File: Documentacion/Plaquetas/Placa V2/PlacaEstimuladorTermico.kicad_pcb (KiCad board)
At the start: 2 copper layers, 207.5 x 149.9 mm, 70 parts, among them J1 Conn_01x02, J2 DB9_Female_MountingHoles, J3 Conn_01x01, J4 Conn_01x01, J5 Conn_01x02, J6 Pulsador OFF, J7 Conn_02x04_Counter_Clockwise, J8 Conn_02x04_Counter_Clockwise, K1 Modulo_Relé, Q1 IRF4905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

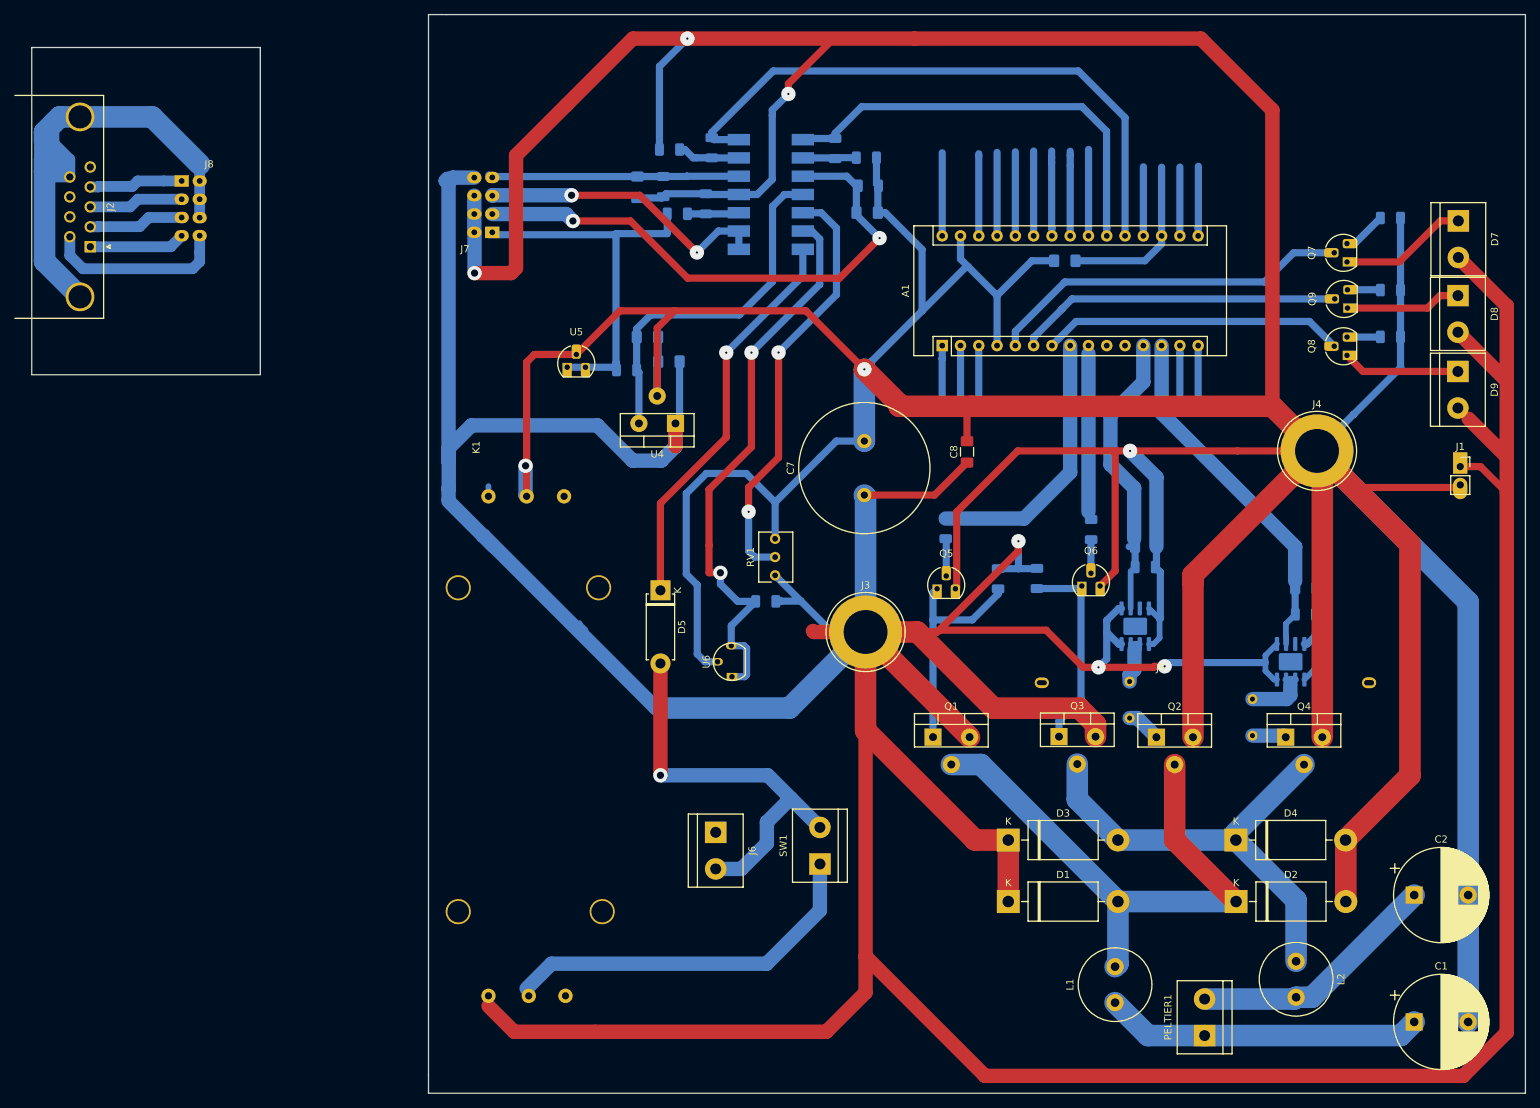
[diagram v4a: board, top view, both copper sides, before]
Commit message: Modification of the main board, add of leds circuit and db9 board
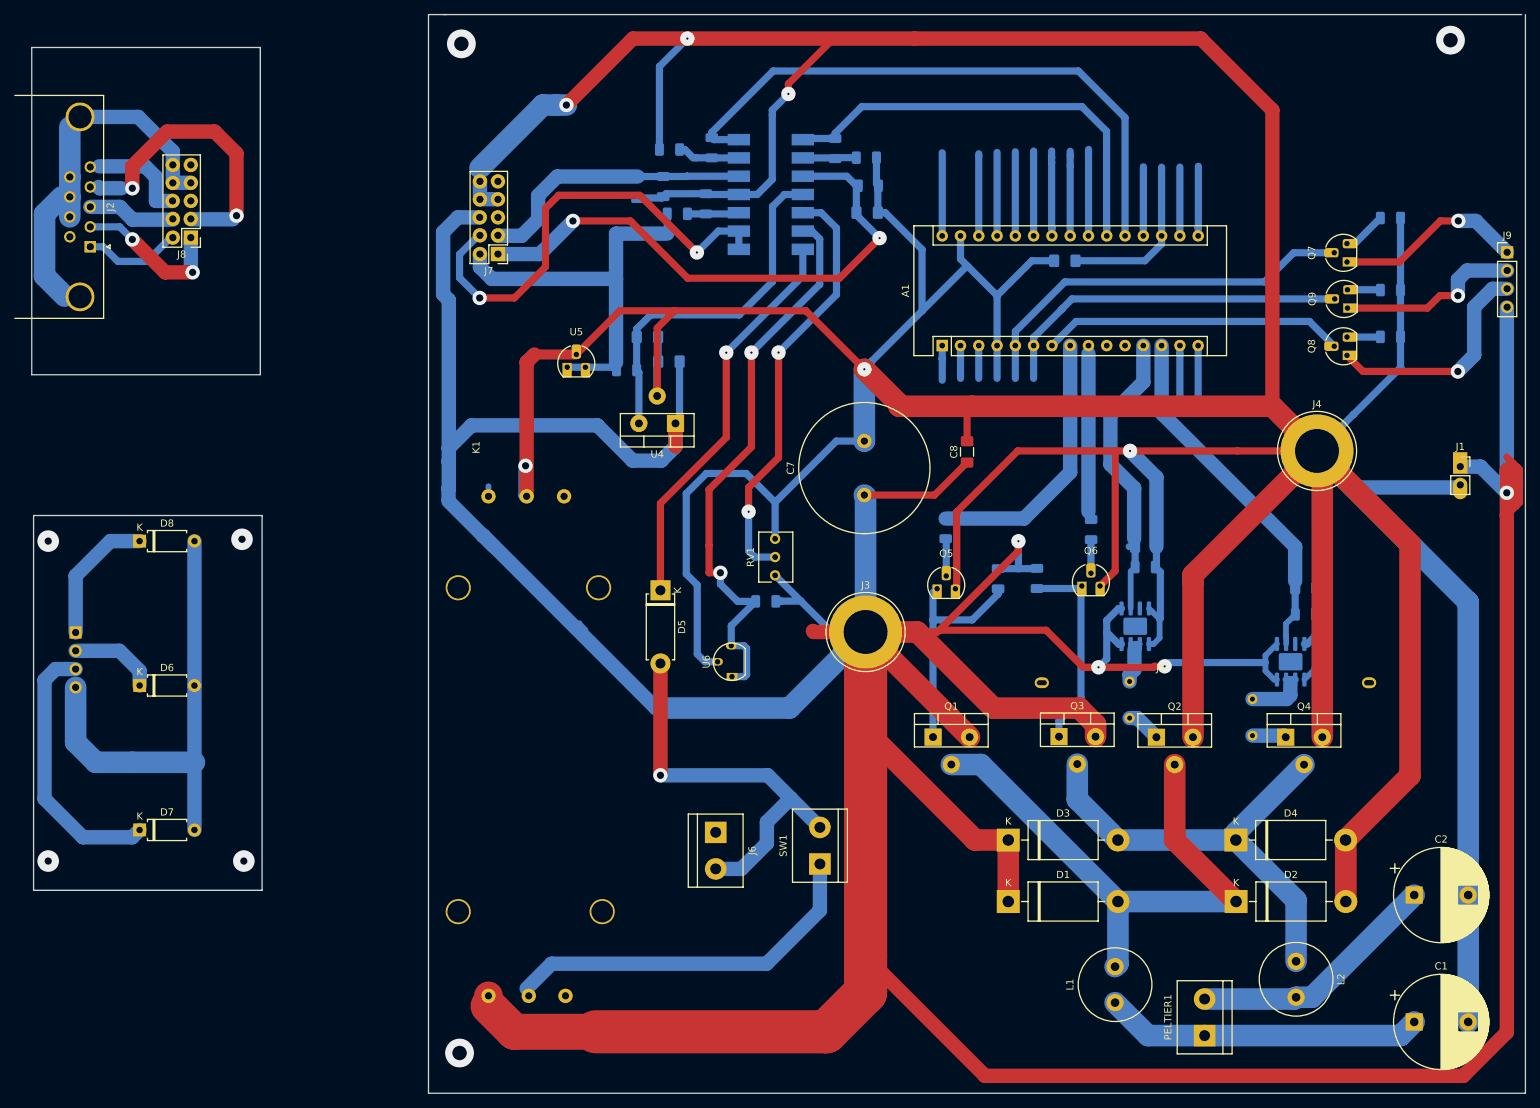
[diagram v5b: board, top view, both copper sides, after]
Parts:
- removed D9: LED, TerminalBlock:TerminalBlock_bornier-2_P5.08mm
- added D6: Yellow, Diode_THT:D_A-405_P7.62mm_Horizontal, F.Cu at (71.6, 105.9)
- added J10: Conn_01x04_Male, Connector_PinHeader_2.54mm:PinHeader_1x04_P2.54mm_Vertical, B.Cu at (62.7, 98.6)
- added J9: Conn_01x04_Male, Connector_PinHeader_2.54mm:PinHeader_1x04_P2.54mm_Vertical, F.Cu at (261.6, 45.7)
- D7: value LED -> Green; footprint TerminalBlock:TerminalBlock_bornier-2_P5.08mm -> Diode_THT:D_A-405_P7.62mm_Horizontal
- D8: value LED -> RED; footprint TerminalBlock:TerminalBlock_bornier-2_P5.08mm -> Diode_THT:D_A-405_P7.62mm_Horizontal
- J7: value Conn_02x04_Counter_Clockwise -> Conn_02x05_Counter_Clockwise; footprint Package_DIP:DoublePin -> Connector_PinHeader_2.54mm:PinHeader_2x05_P2.54mm_VerticalNico
- J8: value Conn_02x04_Counter_Clockwise -> Conn_02x05_Counter_Clockwise; footprint Package_DIP:DoublePin -> Connector_PinHeader_2.54mm:PinHeader_2x05_P2.54mm_Vertical
- R10: value 82k -> 68k
- R17: value R -> 1.5k
- moved D7 201.8 mm to (71.6, 126.0), turned to 0 degrees
- moved D8 186.3 mm to (71.6, 85.9), turned to 0 degrees
- moved J8 7.98 mm to (78.7, 43.7), turned to 180 degrees
- moved J7 3.12 mm to (121.4, 46.0)
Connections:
- A1 pad 29: fan_2 -> GND
- A1 pad 4: fan_2 -> GND
- C1 pad 2: fan_2 -> GND
- C10 pad 2: fan_2 -> GND
- C11 pad 2: fan_2 -> GND
- C2 pad 2: fan_2 -> GND
- C3 pad 2: fan_2 -> GND
- C4 pad 2: fan_2 -> GND
- C5 pad 2: fan_2 -> GND
- C6 pad 2: fan_2 -> GND
- C7 pad 2: fan_2 -> GND
- C8 pad 2: fan_2 -> GND
- C9 pad 2: fan_2 -> GND
- D2 pad 2: fan_2 -> GND
- D4 pad 2: fan_2 -> GND
- D7 pad 2: VCC -> Net-(D6-Pad2)
- D8 pad 2: VCC -> Net-(D6-Pad2)
- J1 pad 2: fan_2 -> GND
- J2 pad 1: term_disip_2C -> term_pelt_1C
- J2 pad 2: term_disip_1C -> term_pelt_2C
- J2 pad 3: term_pelt_2C -> term_disip_1C
- J2 pad 4: term_pelt_1C -> term_disip_2C
- J2 pad 5: Net-(J2-Pad5) -> fan_1C
- J2 pad 6: fan_1C -> Net-(J2-Pad6)
- J2 pad 7: Net-(J2-Pad7) -> fan_2C
- J2 pad 8: Net-(J2-Pad8) -> fan_2C
- J4 pad 1: fan_2 -> GND
- J7 pad 1: REF_OPAMPS -> term_pelt_2
- J7 pad 2: term_pelt_2 -> term_disip_2
- J7 pad 3: term_disip_1 -> Net-(J7-Pad3)
- J7 pad 4: term_disip_2 -> GND
- J7 pad 5: VCC -> Net-(J7-Pad5)
- J7 pad 6: fan_2 -> GND
- J7 pad 7: fan_2 -> GND
- J7 pad 8: fan_2 -> VCC
- J8 pad 1: term_pelt_1C -> term_pelt_2C
- J8 pad 2: term_pelt_2C -> term_disip_2C
- J8 pad 3: term_disip_1C -> Net-(J8-Pad3)
- J8 pad 4: term_disip_2C -> fan_2C
- J8 pad 5: fan_1C -> Net-(J8-Pad5)
- J8 pad 8: fan_2C -> fan_1C
- K1 pad 2: fan_2 -> GND
- Q2 pad 3: fan_2 -> GND
- Q4 pad 3: fan_2 -> GND
- Q5 pad 3: fan_2 -> GND
- Q6 pad 3: fan_2 -> GND
- Q7 pad 1: Net-(D7-Pad1) -> Net-(J9-Pad1)
- Q9 pad 1: Net-(D8-Pad1) -> Net-(J9-Pad2)
- R1 pad 2: fan_2 -> GND
- R18 pad 2: fan_2 -> GND
- R19 pad 2: fan_2 -> GND
- R2 pad 2: fan_2 -> GND
- R20 pad 2: fan_2 -> GND
- R3 pad 2: fan_2 -> GND
- R5 pad 2: fan_2 -> GND
- R7 pad 2: fan_2 -> GND
- R8 pad 2: fan_2 -> GND
- R9 pad 2: fan_2 -> GND
- RV1 pad 1: fan_2 -> GND
- U1 pad 11: fan_2 -> GND
- U2 pad 4: fan_2 -> GND
- U2 pad 5: fan_2 -> GND
- U3 pad 4: fan_2 -> GND
- U3 pad 5: fan_2 -> GND
- U4 pad 2: fan_2 -> GND
- U5 pad 2: fan_2 -> GND
- U6 pad 2: fan_2 -> GND
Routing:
- net fan_2: track 1032.2 -> 0.00 mm, vias 6 -> 0
- net GND: track 0.00 -> 1016.9 mm, vias 0 -> 6
- net Net-(D6-Pad2): track 0.00 -> 65.4 mm
- net term_disip_2C: track 13.3 -> 42.2 mm, vias 0 -> 2
- net Net-(J9-Pad1): track 0.00 -> 26.4 mm, vias 0 -> 1
- net fan_2C: track 81.6 -> 55.4 mm
- net Net-(J9-Pad2): track 0.00 -> 25.7 mm, vias 0 -> 1
- net term_disip_1: track 41.3 -> 64.8 mm
- net Net-(D7-Pad1): track 17.8 -> 37.3 mm
- net Net-(J9-Pad3): track 16.3 -> 31.8 mm, vias 0 -> 1
- net Net-(D6-Pad1): track 0.00 -> 12.1 mm
- net fan_1C: track 25.4 -> 15.4 mm
- net VCC: track 790.5 -> 781.0 mm, vias 3 -> 4
- net term_pelt_2C: track 13.1 -> 22.0 mm, vias 0 -> 2
- net PIN-WARNING-LED-RED: track 50.8 -> 55.4 mm
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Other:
- outline, holes or cut-outs redrawn

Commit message: Add holes to the board
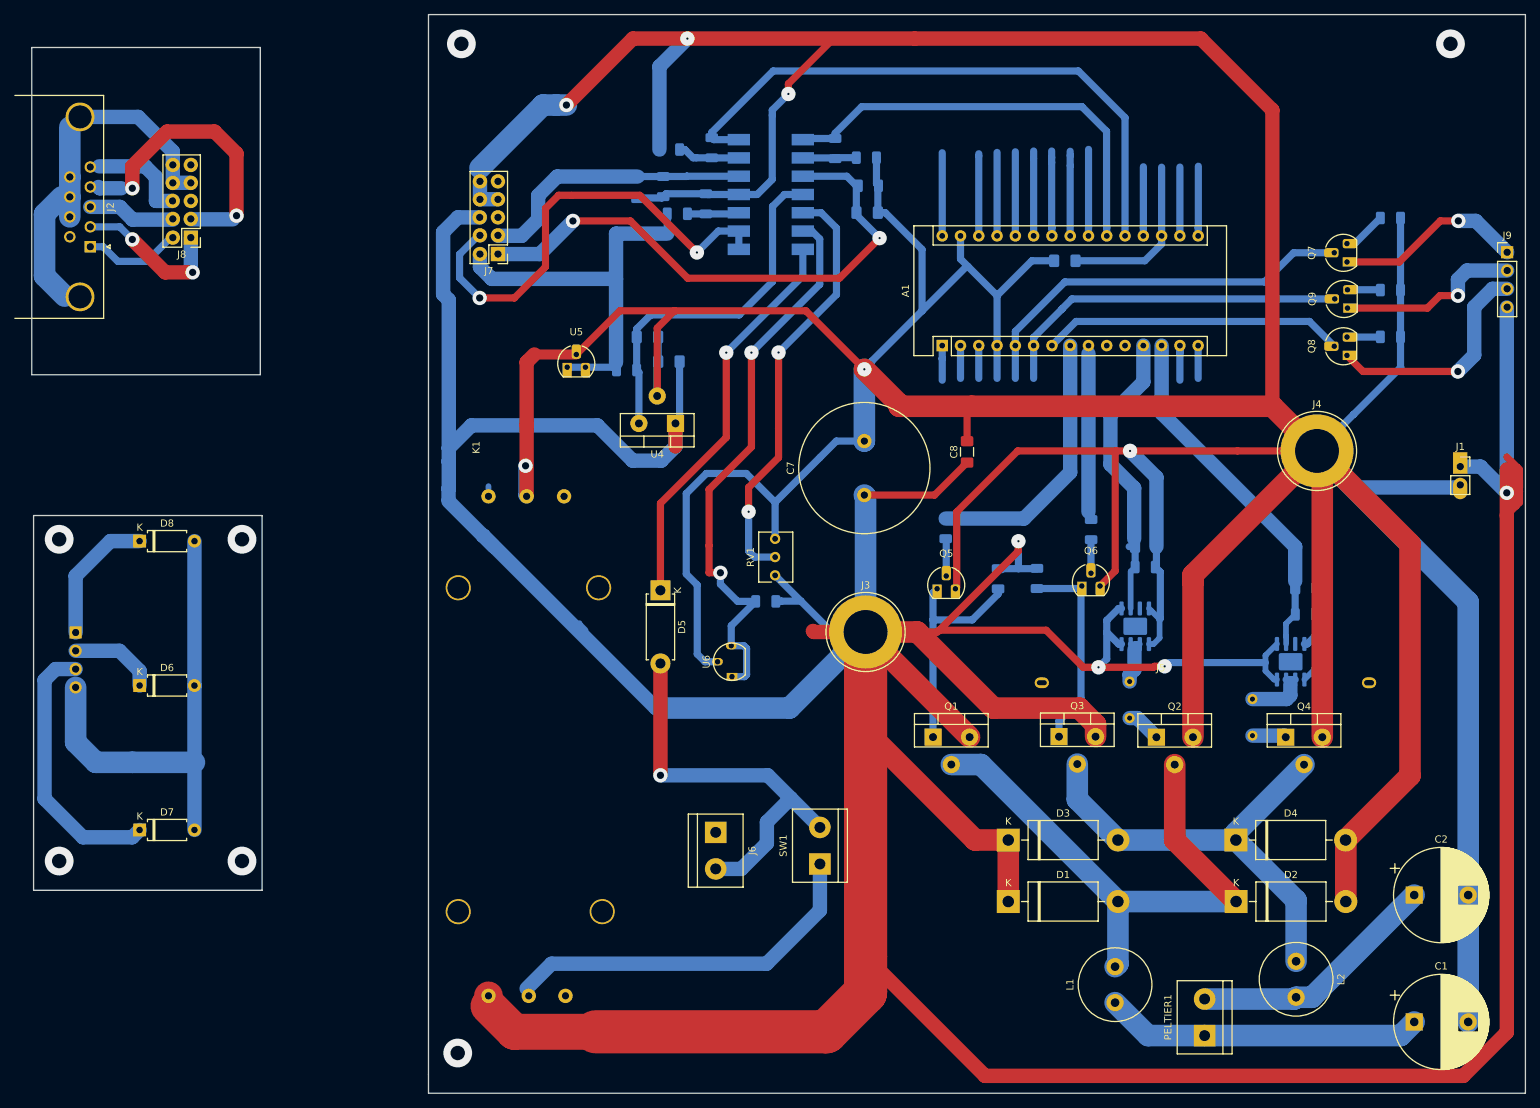
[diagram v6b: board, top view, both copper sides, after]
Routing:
- net Net-(A1-Pad15): track 8.44 -> 4.56 mm
- net Net-(A1-Pad14): track 8.64 -> 5.94 mm
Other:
- outline, holes or cut-outs redrawn
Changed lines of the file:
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@@
   (general
     (thickness 1.4)
-    (drawings 34)
+    (drawings 35)
     (tracks 680)
     (zones 0)
@@
     )
   )
-  (dimension 137.414 (width 0.12) (layer B.SilkS)
-    (gr_text "137,414 mm" (at 185.039 9.652) (layer B.SilkS)
+  (dimension 52.578 (width 0.12) (layer B.SilkS)
+    (gr_text "52,578 mm" (at 29.718 108.585 270) (layer B.SilkS)
       (effects (font (size 1 1) (thickness 0.15)))
     )
-    (feature1 (pts (xy 253.746 13.462) (xy 253.746 10.335579)))
-    (feature2 (pts (xy 116.332 13.462) (xy 116.332 10.335579)))
-    (crossbar (pts (xy 116.332 10.922) (xy 253.746 10.922)))
-    (arrow1a (pts (xy 253.746 10.922) (xy 252.619496 11.508421)))
-    (arrow1b (pts (xy 253.746 10.922) (xy 252.619496 10.335579)))
-    (arrow2a (pts (xy 116.332 10.922) (xy 117.458504 11.508421)))
-    (arrow2b (pts (xy 116.332 10.922) (xy 117.458504 10.335579)))
+    (feature1 (pts (xy 38.862 134.874) (xy 30.401579 134.874)))
+    (feature2 (pts (xy 38.862 82.296) (xy 30.401579 82.296)))
+    (crossbar (pts (xy 30.988 82.296) (xy 30.988 134.874)))
+    (arrow1a (pts (xy 30.988 134.874) (xy 30.401579 133.747496)))
+    (arrow1b (pts (xy 30.988 134.874) (xy 31.574421 133.747496)))
+    (arrow2a (pts (xy 30.988 82.296) (xy 30.401579 83.422504)))
+    (arrow2b (pts (xy 30.988 82.296) (xy 31.574421 83.422504)))
+  )
+  (dimension 137.16 (width 0.12) (layer B.SilkS)
+    (gr_text "137,160 mm" (at 185.166 6.604001) (layer B.SilkS)
+      (effects (font (size 1 1) (thickness 0.15)))
+    )
+    (feature1 (pts (xy 116.586 16.51) (xy 116.586 7.28758)))
+    (feature2 (pts (xy 253.746 16.51) (xy 253.746 7.28758)))
+    (crossbar (pts (xy 253.746 7.874001) (xy 116.586 7.874001)))
+    (arrow1a (pts (xy 116.586 7.874001) (xy 117.712504 7.28758)))
+    (arrow1b (pts (xy 116.586 7.874001) (xy 117.712504 8.460422)))
+    (arrow2a (pts (xy 253.746 7.874001) (xy 252.619496 7.28758)))
+    (arrow2b (pts (xy 253.746 7.874001) (xy 252.619496 8.460422)))
   )
+  (gr_line (start 264.16 12.7) (end 114.3 12.7) (layer Edge.Cuts) (width 0.05))
   (dimension 140.208 (width 0.12) (layer B.SilkS)
     (gr_text "140,208 mm" (at 109.728 86.868 270) (layer B.SilkS)
@@
   (gr_line (start 111.76 12.7) (end 111.76 160.02) (layer Edge.Cuts) (width 0.05))
   (gr_line (start 114.3 12.7) (end 111.76 12.7) (layer Edge.Cuts) (width 0.05))
-  (gr_line (start 263.652 12.7) (end 113.792 12.7) (layer Edge.Cuts) (width 0.05))
   (gr_text "DB9\nPELTIER" (at -33.38068 106.38536 90) (layer Dwgs.User)
     (effects (font (size 10 10) (thickness 0.15)))
@@
     (arrow2b (pts (xy 182.54972 102.64022) (xy 183.676224 102.053799)))
   )
-  (via (at 58.928 85.852) (size 3) (drill 1) (layers F.Cu B.Cu) (net 0))
-  (via (at 58.928 130.302) (size 3) (drill 1) (layers F.Cu B.Cu) (net 0))
-  (via (at 86.106 130.302) (size 3) (drill 1) (layers F.Cu B.Cu) (net 0))
-  (via (at 85.852 85.598) (size 3) (drill 1) (layers F.Cu B.Cu) (net 0))
+  (via (at 60.452 85.598) (size 4) (drill 2) (layers F.Cu B.Cu) (net 0))
+  (via (at 60.452 130.302) (size 4) (drill 2) (layers F.Cu B.Cu) (net 0))
+  (via (at 85.852 130.302) (size 4) (drill 2) (layers F.Cu B.Cu) (net 0))
+  (via (at 85.852 85.598) (size 4) (drill 2) (layers F.Cu B.Cu) (net 0))
   (via (at 116.332 16.764) (size 4) (drill 2) (layers F.Cu B.Cu) (net 0))
-  (via (at 116.078 156.972) (size 4) (drill 2) (layers F.Cu B.Cu) (net 0))
-  (via (at 253.746 16.256) (size 4) (drill 2) (layers F.Cu B.Cu) (net 0))
+  (via (at 115.824 156.972) (size 4) (drill 2) (layers F.Cu B.Cu) (net 0))
+  (via (at 253.746 16.764) (size 4) (drill 2) (layers F.Cu B.Cu) (net 0))
   (segment (start 218.694 42.31533) (end 218.7194 42.28993) (width 1) (layer B.Cu) (net 1))
   (segment (start 218.694 43.4467) (end 218.694 42.31533) (width 1) (layer B.Cu) (net 1))
@@
   (segment (start 183.134 43.4467) (end 183.134 31.89478) (width 1) (layer B.Cu) (net 3))
   (segment (start 216.154 58.6867) (end 216.154 59.81807) (width 1) (layer B.Cu) (net 4))
-  (segment (start 216.154 59.81807) (end 216.154 67.32778) (width 1) (layer B.Cu) (net 4))
+  (segment (start 216.154 58.6867) (end 216.154 63.5) (width 1) (layer B.Cu) (net 4))
   (segment (start 188.214 32.32658) (end 188.214 32.03194) (width 1) (layer B.Cu) (net 5))
   (segment (start 188.214 43.4467) (end 188.214 32.32658) (width 1) (layer B.Cu) (net 5))
@@
   (segment (start 160.39592 74.23658) (end 160.39592 70.1675) (width 1) (layer F.Cu) (net 54))
   (segment (start 156.2354 78.3971) (end 160.39592 74.23658) (width 1) (layer F.Cu) (net 54))
-  (segment (start 218.694 58.6867) (end 218.694 67.12458) (width 1) (layer B.Cu) (net 57))
+  (segment (start 218.694 58.6867) (end 218.694 63.246) (width 1) (layer B.Cu) (net 57))
   (segment (start 230.90964 105.08982) (end 232.17964 105.08982) (width 1) (layer B.Cu) (net 60))
   (segment (start 226.2378 107.7976) (end 230.9876 107.7976) (width 2) (layer B.Cu) (net 60))
@@
   (segment (start 159.52216 35.60302) (end 159.52216 26.69032) (width 1) (layer B.Cu) (net 74))
   (via (at 147.72894 16.03502) (size 2) (drill 0.3) (layers F.Cu B.Cu) (net 74))
-  (segment (start 143.84736 19.9166) (end 147.72894 16.03502) (width 1) (layer B.Cu) (net 74))
-  (segment (start 143.84736 31.44774) (end 143.84736 19.9166) (width 1) (layer B.Cu) (net 74))
+  (segment (start 143.84736 19.9166) (end 147.72894 16.03502) (width 2) (layer B.Cu) (net 74))
+  (segment (start 143.84736 31.44774) (end 143.84736 19.9166) (width 2) (layer B.Cu) (net 74))
   (segment (start 147.72894 16.03502) (end 140.15668 16.03502) (width 2) (layer F.Cu) (net 74))
   (via (at 161.76244 23.72868) (size 2) (drill 0.3) (layers F.Cu B.Cu) (net 74))
